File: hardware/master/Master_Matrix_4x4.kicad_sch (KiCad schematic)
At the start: 43 parts, among them U1 ESP32-DevKit-V1-30Pin, U2 74AHCT1G125

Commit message: feat(hardware): update Master 4x4 schematic, export PDF, add PCB layout and libraries
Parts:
- removed J_WEST: Mag_West (Male), Library:fakemag4pin90degMale, symbol New_Library:fakeMag4pinMale
- removed MOD1, MOD10, MOD11, MOD12, MOD13, MOD14, MOD15, MOD16, MOD2, MOD3, MOD4, MOD5, MOD6, MOD7, MOD8, MOD9: WCMCU-2812-4, Module:CJMCU-2812-4, symbol Custom:CJMCU-2812-4
- removed U1: ESP32-DevKit-V1-30Pin, Module:ESP32-DevKit-V1-30Pin, symbol Module:ESP32-DevKit-V1-30Pin
- added C_BULK1: 100uF, Capacitor_SMD:C_1206_3216Metric, symbol Device:C
- added D_TVS1: SMAJ5.0A, Diode_SMD:D_SMA, symbol Device:D_TVS
- added MOD1, MOD10, MOD11, MOD12, MOD13, MOD14, MOD15, MOD16, MOD2, MOD3, MOD4, MOD5, MOD6, MOD7, MOD8, MOD9: WS2812_Matrix_2x2, ws2812-matrix-2x2:WS2812_Matrix_2x2_15x15mm, symbol ws2812-matrix-2x2:WS2812_Matrix_2x2
- added R_CC1, R_CC2: 5.1k, Resistor_SMD:R_0603_1608Metric, symbol Device:R
- added SW1: SW_SPDT, Button_Switch_SMD:SW_SPDT_PCM12, symbol Switch:SW_SPDT
- added U1: esp32-wemos-d1-mini, esp32-wemos-d1-mini:esp32-wemos-d1-mini, symbol esp32-wemos-d1-mini:esp32-wemos-d1-mini
- C_MOD1, C_MOD10, C_MOD11, C_MOD12, C_MOD13, C_MOD14, C_MOD15, C_MOD16, C_MOD2, C_MOD3, C_MOD4, C_MOD5, C_MOD6, C_MOD7, C_MOD8, C_MOD9: footprint Capacitor_SMD:C_0603_1608Metric -> Capacitor_SMD:C_0805_2012Metric
- J_PWR1: renamed from J_PWR; value DC_5V_IN -> USB_C_6P_3A_5V_IN; footprint TerminalBlock:TerminalBlock_bornier-2_P5.08mm -> Connector_USB:USB_C_Receptacle_6P_SMD; symbol Connector_Generic:Conn_01x02 -> Connector_USB:USB_C_Receptacle_6P; MPN TB002-508-02BE -> TYPE-C-6P-SMD
- U2: MPN SN74AHCT1G125DBVR -> OS102011MA1QN1
- renumbered J_EAST to J_EAST1, J_NORTH to J_NORTH1, J_SOUTH to J_SOUTH1
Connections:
- net +3V3: now also U1.16 (3V3)
- net +5V: now also C_BULK1.1, MOD1.2 (VCC_IN), MOD1.6 (VCC_OUT), MOD10.2 (VCC_IN), MOD10.6 (VCC_OUT), MOD11.2 (VCC_IN), MOD11.6 (VCC_OUT), MOD12.2 (VCC_IN), MOD12.6 (VCC_OUT), MOD13.2 (VCC_IN), MOD13.6 (VCC_OUT), MOD14.2 (VCC_IN), MOD14.6 (VCC_OUT), MOD15.2 (VCC_IN), MOD15.6 (VCC_OUT), MOD16.2 (VCC_IN), MOD16.6 (VCC_OUT), MOD2.2 (VCC_IN), MOD2.6 (VCC_OUT), MOD3.2 (VCC_IN), MOD3.6 (VCC_OUT), MOD4.2 (VCC_IN), MOD4.6 (VCC_OUT), MOD5.2 (VCC_IN), MOD5.6 (VCC_OUT), MOD6.2 (VCC_IN), MOD6.6 (VCC_OUT), MOD7.2 (VCC_IN), MOD7.6 (VCC_OUT), MOD8.2 (VCC_IN), MOD8.6 (VCC_OUT), MOD9.2 (VCC_IN), MOD9.6 (VCC_OUT), SW1.2 (B), U1.35 (VCC_(USB)); no longer C_MOD1.1, C_MOD10.1, C_MOD11.1, C_MOD12.1, C_MOD13.1, C_MOD14.1, C_MOD15.1, C_MOD16.1, C_MOD2.1, C_MOD3.1, C_MOD4.1, C_MOD5.1, C_MOD6.1, C_MOD7.1, C_MOD8.1, C_MOD9.1, J_PWR1.1 (Pin_1)
- net D01: now also U1.6 (IO_26/D0)
- net D11: now also U1.13 (IO_14/TMS)
- net D21: now also U1.18 (IO_13/TCK)
- net DIN: now also MOD1.3 (DIN)
- net DOUT: now also MOD16.7 (DOUT)
- net GND: now also J_PWR1.1 (GND), J_PWR1.6 (GND), J_PWR1.SH, C_BULK1.2, D_TVS1.2 (A2), MOD1.1 (GND_IN1), MOD1.4 (GND_IN2), MOD1.5 (GND_OUT1), MOD1.8 (GND_OUT2), MOD10.1 (GND_IN1), MOD10.4 (GND_IN2), MOD10.5 (GND_OUT1), MOD10.8 (GND_OUT2), MOD11.1 (GND_IN1), MOD11.4 (GND_IN2), MOD11.5 (GND_OUT1), MOD11.8 (GND_OUT2), MOD12.1 (GND_IN1), MOD12.4 (GND_IN2), MOD12.5 (GND_OUT1), MOD12.8 (GND_OUT2), MOD13.1 (GND_IN1), MOD13.4 (GND_IN2), MOD13.5 (GND_OUT1), MOD13.8 (GND_OUT2), MOD14.1 (GND_IN1), MOD14.4 (GND_IN2), MOD14.5 (GND_OUT1), MOD14.8 (GND_OUT2), MOD15.1 (GND_IN1), MOD15.4 (GND_IN2), MOD15.5 (GND_OUT1), MOD15.8 (GND_OUT2), MOD16.1 (GND_IN1), MOD16.4 (GND_IN2), MOD16.5 (GND_OUT1), MOD16.8 (GND_OUT2), MOD2.1 (GND_IN1), MOD2.4 (GND_IN2), MOD2.5 (GND_OUT1), MOD2.8 (GND_OUT2), MOD3.1 (GND_IN1), MOD3.4 (GND_IN2), MOD3.5 (GND_OUT1), MOD3.8 (GND_OUT2), MOD4.1 (GND_IN1), MOD4.4 (GND_IN2), MOD4.5 (GND_OUT1), MOD4.8 (GND_OUT2), MOD5.1 (GND_IN1), MOD5.4 (GND_IN2), MOD5.5 (GND_OUT1), MOD5.8 (GND_OUT2), MOD6.1 (GND_IN1), MOD6.4 (GND_IN2), MOD6.5 (GND_OUT1), MOD6.8 (GND_OUT2), MOD7.1 (GND_IN1), MOD7.4 (GND_IN2), MOD7.5 (GND_OUT1), MOD7.8 (GND_OUT2), MOD8.1 (GND_IN1), MOD8.4 (GND_IN2), MOD8.5 (GND_OUT1), MOD8.8 (GND_OUT2), MOD9.1 (GND_IN1), MOD9.4 (GND_IN2), MOD9.5 (GND_OUT1), MOD9.8 (GND_OUT2), R_CC1.2, R_CC2.2, U1.1 (GND), U1.22 (GND), U1.33 (GND); no longer C_MOD1.2, C_MOD10.2, C_MOD11.2, C_MOD12.2, C_MOD13.2, C_MOD14.2, C_MOD15.2, C_MOD16.2, C_MOD2.2, C_MOD3.2, C_MOD4.2, C_MOD5.2, C_MOD6.2, C_MOD7.2, C_MOD8.2, C_MOD9.2, J_PWR1.2 (Pin_2)
- net DIN_3V3: now reaches U2.2 (A)
- net DIN_3V3: now also U1.8 (IO_18/D5)
- net at R2.2: now also U1.2 (RST)
- new net: MOD13.7 (DOUT), MOD14.3 (DIN)
- new net: MOD14.7 (DOUT), MOD15.3 (DIN)
- new net: MOD10.3 (DIN), MOD9.7 (DOUT)
- new net: MOD10.7 (DOUT), MOD11.3 (DIN)
- new net: MOD5.7 (DOUT), MOD6.3 (DIN)
- new net: MOD1.7 (DOUT), MOD2.3 (DIN)
- new net: MOD2.7 (DOUT), MOD3.3 (DIN)
- new net: MOD3.7 (DOUT), MOD4.3 (DIN)
- new net: MOD15.7 (DOUT), MOD16.3 (DIN)
- new net: MOD7.7 (DOUT), MOD8.3 (DIN)
- new net: MOD11.7 (DOUT), MOD12.3 (DIN)
- new net: MOD6.7 (DOUT), MOD7.3 (DIN)
- new net CC1: J_PWR1.3 (CC1), R_CC1.1
- new net CC2: J_PWR1.4 (CC2), R_CC2.1
- new net DOUT12: MOD12.7 (DOUT), MOD13.3 (DIN)
- new net DOUT4: MOD4.7 (DOUT), MOD5.3 (DIN)
- new net DOUT8: MOD8.7 (DOUT), MOD9.3 (DIN)
- new net VBUS_IN: D_TVS1.1 (A1), J_PWR1.2 (VBUS), J_PWR1.5 (VBUS), SW1.1 (A)
- no-connect marks 20 -> 31

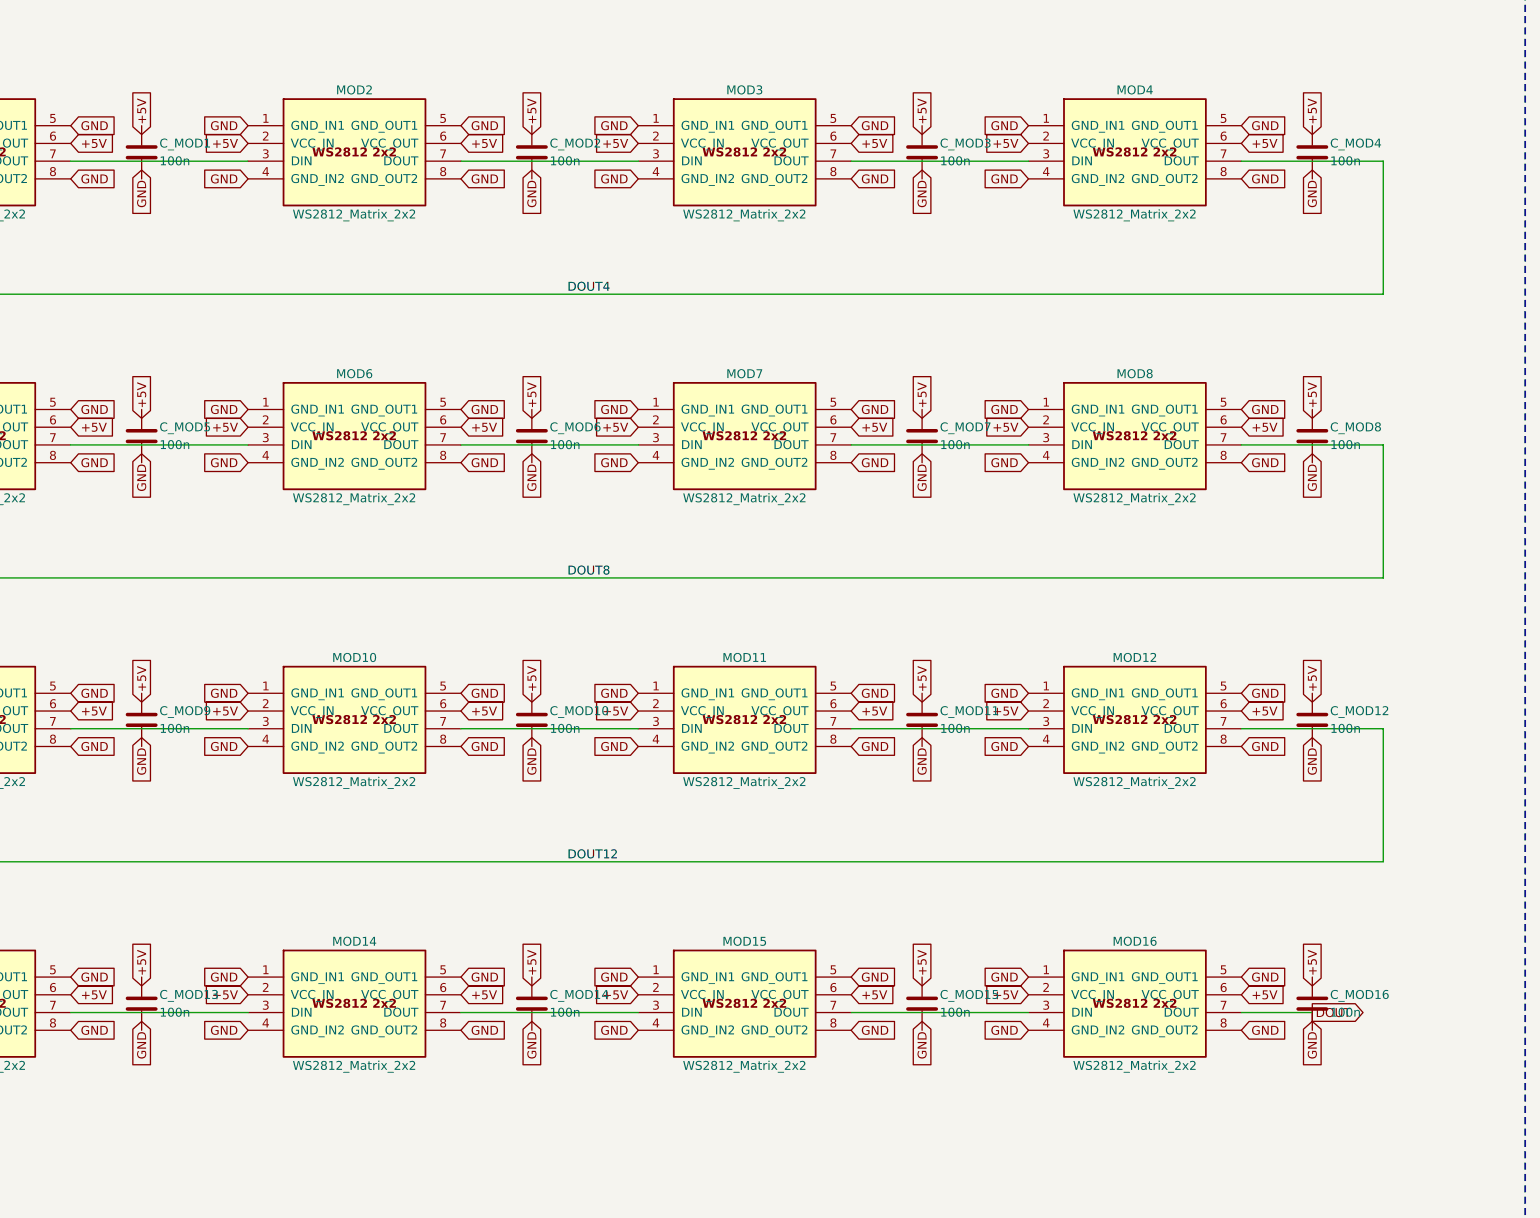
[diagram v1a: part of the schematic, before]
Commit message: feat(hardware): update Master PCB layout and Master/Slave 4x4 matrix schematics
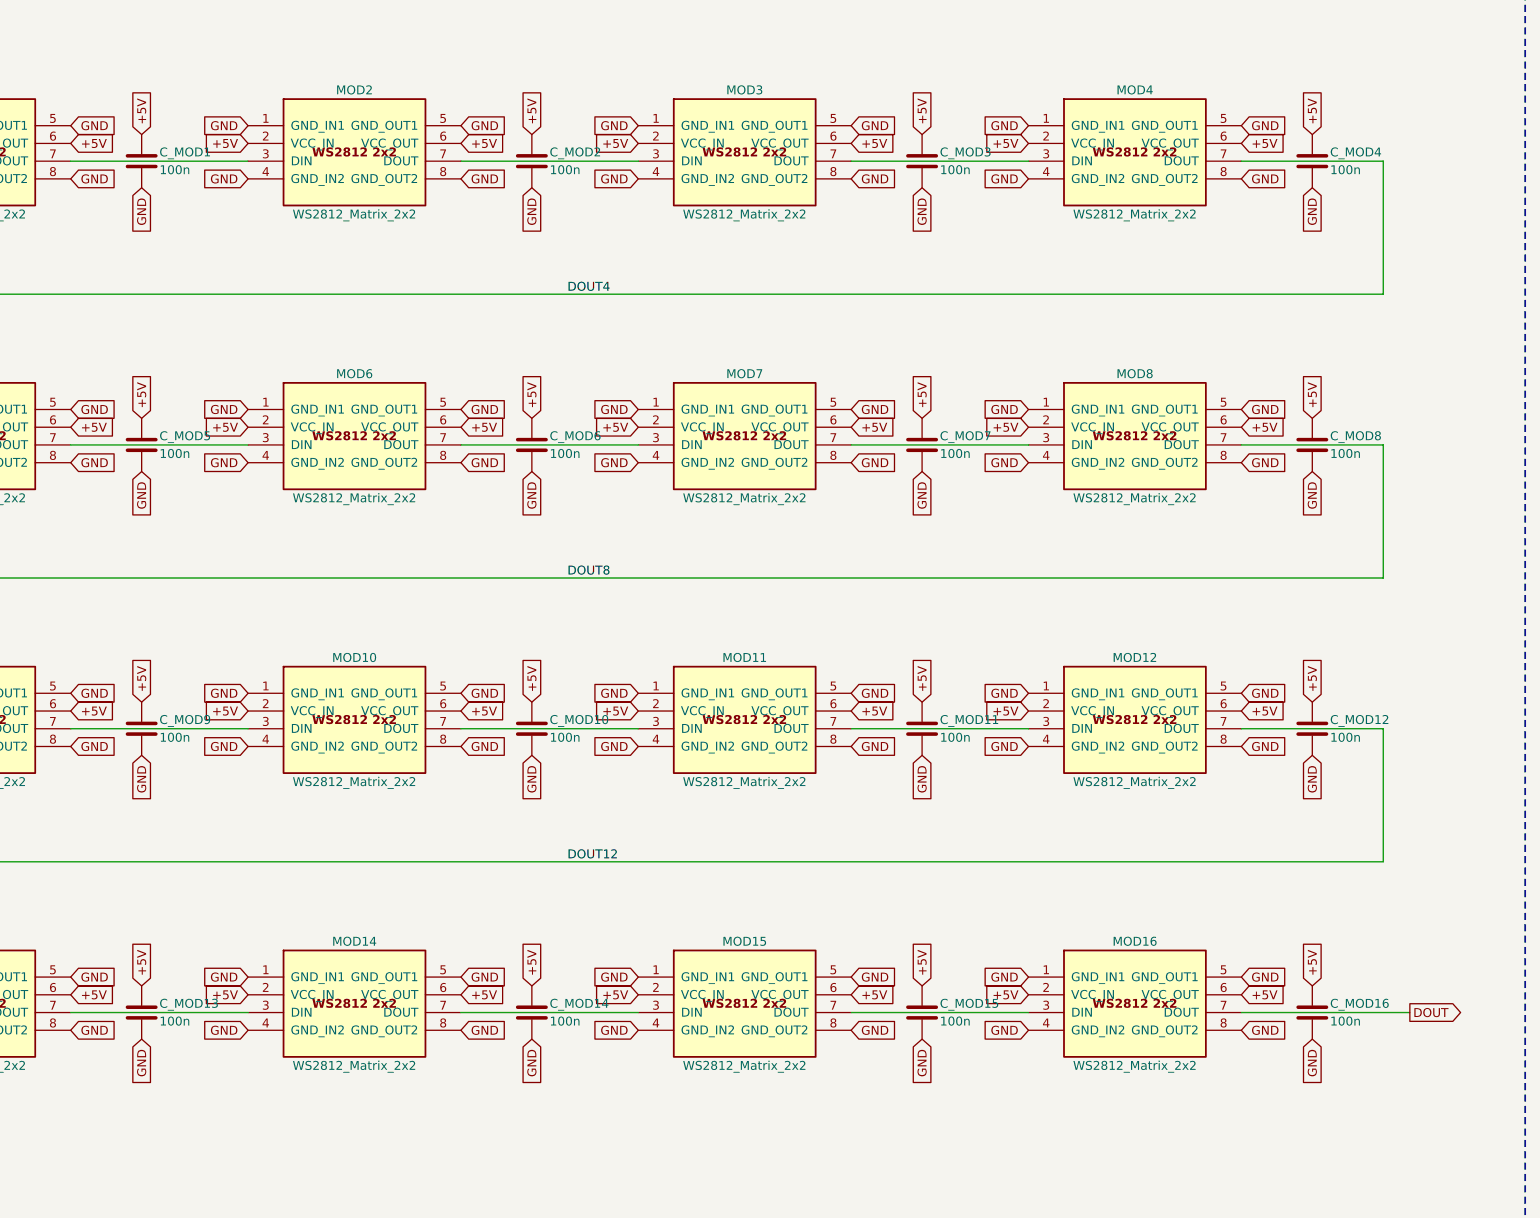
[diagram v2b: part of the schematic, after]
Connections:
- net +5V: now also C_MOD1.1, C_MOD10.1, C_MOD11.1, C_MOD12.1, C_MOD13.1, C_MOD14.1, C_MOD15.1, C_MOD16.1, C_MOD2.1, C_MOD3.1, C_MOD4.1, C_MOD5.1, C_MOD6.1, C_MOD7.1, C_MOD8.1, C_MOD9.1
- net GND: now also C_MOD1.2, C_MOD10.2, C_MOD11.2, C_MOD12.2, C_MOD13.2, C_MOD14.2, C_MOD15.2, C_MOD16.2, C_MOD2.2, C_MOD3.2, C_MOD4.2, C_MOD5.2, C_MOD6.2, C_MOD7.2, C_MOD8.2, C_MOD9.2
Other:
- moved on the sheet: C_MOD1, C_MOD10, C_MOD11, C_MOD12, C_MOD13, C_MOD14, C_MOD15, C_MOD16, C_MOD2, C_MOD3, C_MOD4, C_MOD5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

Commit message: feat(hardware): update schematics, symbol libraries, and system architecture docs
- Update Master and Slave 4x4 matrix schematics with proper data flow pipeline and symbol pinouts
- Align symbol libraries (esp32-wemos-d1-mini, ws2812-matrix-2x2) across common and local folders
- Update project README and hardware documentation for VBUS power distribution, level shifting, and data flow architecture
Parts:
- added C3: 100n, Capacitor_SMD:C_0805_2012Metric, symbol Device:C
- added C4: 1uF, Capacitor_SMD:C_0805_2012Metric, symbol Device:C
- added C_ATTINY, C_INA: 100n, Capacitor_SMD:C_0603_1608Metric, symbol Device:C
- added J_PROG_M: UPDI_PROG, Connector_PinHeader_2.54mm:PinHeader_1x03_P2.54mm_Vertical, symbol Connector_Generic:Conn_01x03
- added R3: 10k, Resistor_SMD:R_0603_1608Metric, symbol Device:R
- added R4: 20k, Resistor_SMD:R_0603_1608Metric, symbol Device:R
- added R5, R6: 4.7k, Resistor_SMD:R_0603_1608Metric, symbol Device:R
- added R_BUS: DNP, Resistor_SMD:R_2512_6332Metric, symbol Device:R
- added R_SHUNT: 0.01R 2W, Resistor_SMD:R_2512_6332Metric, symbol Device:R
- added U_ATTINY: ATtiny1604-SS, Package_SO:SOIC-14_3.9x8.7mm_P1.27mm, symbol MCU_Microchip_ATtiny:ATtiny1604-SS
- added U_INA: INA219AxD, Package_SO:SOIC-8_3.9x4.9mm_P1.27mm, symbol Sensor_Energy:INA219AxD
- D_TVS1: value SMAJ5.0A -> D_TVS
- U2: MPN OS102011MA1QN1 -> 74AHCT1G125GV,125
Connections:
- net +3V3: now also R2.2, C_INA.1, R5.1, R6.1, U_INA.5 (VS); no longer R2.1
- net +5V: now also C_ATTINY.1, J_PROG_M.3 (Pin_3), R_BUS.1, U_ATTINY.1 (VCC); no longer J_EAST1.4, J_NORTH1.4, J_SOUTH1.1, U1.35 (VCC_(USB))
- net GND: now also J_SOUTH1.1, C3.2, C4.2, C_ATTINY.2, C_INA.2, J_PROG_M.2 (Pin_2), R4.2, U_ATTINY.14 (GND), U_INA.1 (A1), U_INA.2 (A0), U_INA.6 (GND); no longer J_SOUTH1.4
- net VBUS_IN: now also C3.1, C4.1, R_SHUNT.1, U_INA.8 (VIN+); no longer SW1.1 (A)
- net ESP_TX_TINY: now reaches U2.4 (Y)
- net ESP_TX_TINY: now also U_ATTINY.6 (PB3); no longer R1.1
- net at U1.2 (RST): now also R2.1; no longer R2.2
- net I2C_SCL: now reaches U1.25 (IO_22/D1/SCL)
- net I2C_SCL: now also R6.2, U_INA.4 (SCL)
- net I2C_SDA: now reaches U1.27 (IO_21/D2/SDA)
- net I2C_SDA: now also R5.2, U_INA.3 (SDA)
- net ESP_TX_3V3: now reaches U1.29 (IO_17/D3)
- net ESP_TX_3V3: now also U2.2 (A)
- net TINY_TX_ESP: now reaches U1.31 (IO_16/D4)
- net TINY_TX_ESP: now also R3.2, R4.1
- net D01: no longer names the net of U1.6 (IO_26/D0)
- net D01: no longer J_NORTH1.2
- net D11: no longer names the net of U1.13 (IO_14/TMS)
- net D11: no longer J_EAST1.2
- net D21: no longer names the net of U1.18 (IO_13/TCK)
- net D21: no longer J_SOUTH1.3
- net DIN_3V3: no longer names the net of U1.8 (IO_18/D5)
- net DIN_3V3: no longer U2.2 (A)
- net DOUT renamed LINK_TX
- net LINK_TX: now also U_ATTINY.7 (PB2); no longer MOD16.7 (DOUT)
- new net LED_DATA: R1.1, U_ATTINY.9 (PB0)
- new net LINK_RX_E: J_EAST1.2, U_ATTINY.12 (PA2)
- new net LINK_RX_N: J_NORTH1.2, U_ATTINY.11 (PA1)
- new net LINK_RX_S: J_SOUTH1.3, U_ATTINY.13 (PA3)
- new net TINY_TX_5V: R3.1, U_ATTINY.8 (PB1)
- new net UPDI_DATA_M: J_PROG_M.1 (Pin_1), U_ATTINY.10 (~{RESET}/PA0)
- new net VBUS: J_EAST1.4, J_NORTH1.4, J_SOUTH1.4, R_BUS.2
- new net VBUS_SW: R_SHUNT.2, SW1.1 (A), U_INA.7 (VIN-)
- no-connect marks 31 -> 37
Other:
- note added: "1. DUAL-MCU (ESP32 + ATTINY1604) & LEVEL SHIFTER"
- note added: "2. POWER INPUT, PROTECTION & CURRENT SENSING"
- note added: "3. MAGNETIC EDGE CONNECTORS (3-EDGE POKA-YOKE LINK BUS)"
- note removed: "1. ESP32 CONTROLLER & LEVEL SHIFTER"
- note removed: "2. POWER SOURCES & DC INPUT"
- note removed: "3. MAGNETIC EDGE CONNECTORS (SYMMETRICAL MATING & DOUT STREAM)"
- moved on the sheet: C1, C2, C_BULK1, D_TVS1, J_PWR1, R1, R2, R_CC1, R_CC2, SW1, U1, U2
